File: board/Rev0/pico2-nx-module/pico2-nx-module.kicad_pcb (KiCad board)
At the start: 2 copper layers, 89 x 83 mm, 242 parts, among them IC1 LP5810ADSDR, J1 USB_C_Receptacle_USB2.0, J10 FTSH-105-01-L-DV-007-K, J11 Conn_02x06_Odd_Even, J12 Conn_02x03_Odd_Even, J13 Conn_02x03_Odd_Even, J14 Conn_02x03_Odd_Even, J15 Conn_02x03_Odd_Even, J16 Conn_02x06_Odd_Even, J17 Conn_02x06_Odd_Even, J18 100 mil, J2 SM03B-SRSS-TB, J3 SFV22R-2STE1HLF, J4 SFV22R-2STE1HLF, J5 Conn_02x06_Odd_Even, J6 Conn_02x06_Odd_Even, J7 SM04B-SRSS-TB, J8 Conn_02x06_Odd_Even, J9 SM04B-SRSS-TB, Q1 BSS84, SW1 CS1213AGF260, SW2 CS1213AGF260, U1 MIC2005A-2YM5-TR, U10 W25Q32JVSSIQ, U11 RP2350_80QFN, U14 74LV4066, U15 TXS0108EPW, U16 TXS0108EPW, U17 SN74CB3Q3257, U2 MIC2005A-2YM5-TR, U3 LIFCL-17-7MG121C, U4 W25Q128JVSSIQ, U5 APS6408L-OBM-BA, U8 TXS0108EPW, U9 APS6404L-3SQN-SN, Y1 SG-210STF 24.0000ML0, Y2 ABM8-272-T3

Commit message: layout update
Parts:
- removed C1, C2, C4, C5, C75, C82: 10u, Capacitor_SMD:C_0402_1005Metric
- removed C16, C17, C19, C49, C52, C59, C60, C63, C65, C66, C67, C69, C70, C71, C72, C73, C74, C77, C78, C79, C80, C85: 0.1u, Capacitor_SMD:C_0201_0603Metric
- removed C50, C53, C54, C57, C58, C61, C62, C64, C68: 4.7u, Capacitor_SMD:C_0402_1005Metric
- removed C55, C56: 15p, Capacitor_SMD:C_0201_0603Metric
- removed D1, D2, D6: 1N5819WS, Diode_SMD:D_SOD-323
- removed D10: PRTR5V0U2X, Package_TO_SOT_SMD:SOT-143
- removed D3, D5: LTST-C191KGKT, LED_SMD:LED_0603_1608Metric
- removed D4, D7: MHPA1010RGBDT, Piconx3_lib:LED_Cree-PLCC4_1x1mm_CW
- removed FB1: BLM15AG121SN1D, jrt:IND_BLM15_0402_MUR-M
- removed IC1: LP5810ADSDR, jrt:DSD0008B-MFG
- removed J1: USB_C_Receptacle_USB2.0, Connector_USB:USB_C_Receptacle_HRO_TYPE-C-31-M-12
- removed J10: FTSH-105-01-L-DV-007-K, Piconx3_lib:SAMTEC_FTSH-105-X-X-DV-007-P-X_cust
- removed J11, J16, J17, J5, J6, J8: Conn_02x06_Odd_Even, jrt:SAMTEC_HMTSW-106-XX-X-D-XXX
- removed J12, J13, J14, J15: Conn_02x03_Odd_Even, Connector_PinHeader_2.54mm:PinHeader_2x03_P2.54mm_Vertical
- removed J18: 100 mil, Connector_PinHeader_2.54mm:PinHeader_2x05_P2.54mm_Vertical
- removed J4: SFV22R-2STE1HLF, Piconx3_lib:AMPHENOL_SFV22R-2STE1HLF
- removed J7, J9: SM04B-SRSS-TB, Connector_JST:JST_SH_SM04B-SRSS-TB_1x04-1MP_P1.00mm_Horizontal
- removed JP1, JP2, JP3, JP6, JP7: SolderJumper_3_Bridged12, Jumper:SolderJumper-3_P1.3mm_Bridged12_RoundedPad1.0x1.5mm
- removed JP10, JP11, JP12, JP13, JP14, JP4, JP5, JP8, JP9: SolderJumper_2_Bridged, Jumper:SolderJumper-2_P1.3mm_Bridged_RoundedPad1.0x1.5mm
- removed JP15: SolderJumper_2_Open, Jumper:SolderJumper-2_P1.3mm_Open_RoundedPad1.0x1.5mm
- removed L1, L2: 1u, Piconx3_lib:DFE201610E
- removed L4: 3.3u, Piconx3_lib:INDC2016X100N
- removed PS1, PS2, PS3: AP61100QZ6-7, Piconx3_lib:SOT50P160X60-6N
- removed PTC1: MF-FSMF035X-2, Resistor_SMD:R_0603_1608Metric
- removed Q1: BSS84, Package_TO_SOT_SMD:SOT-23
- removed R1, R2, R28, R29, R30, R31, R32, R4, R40, R42, R50, R55, R60, R63, R70, R71: 10K, Resistor_SMD:R_0402_1005Metric
- removed R10, R13, R15, R16, R5, R59, R6, R7: 4.7K, Resistor_SMD:R_0402_1005Metric
- removed R11, R41, R49: 2.2K, Resistor_SMD:R_0402_1005Metric
- removed R14, R21, R23, R25, R52, R61, R64, R65, R66, R67, R75: 200K, Resistor_SMD:R_0402_1005Metric
- removed R17, R35: DNF, Resistor_SMD:R_0402_1005Metric
- removed R19, R20: 0, Resistor_SMD:R_0402_1005Metric
- removed R22: 100K, Resistor_SMD:R_0402_1005Metric
- removed R24: 44.2K, Resistor_SMD:R_0402_1005Metric
- removed R27, R44, R53, R54: 27, Resistor_SMD:R_0402_1005Metric
- removed R34, R45, R46, R47, R48, R56, R57, R58: 1K, Resistor_SMD:R_0402_1005Metric
- removed R36, R38: 56K, Resistor_SMD:R_0402_1005Metric
- removed R37, R39: 5.1K, Resistor_SMD:R_0402_1005Metric
- removed R43, R72, R76, R77, R79: 100, Resistor_SMD:R_0402_1005Metric
- removed R68, R69: 200, Resistor_SMD:R_0402_1005Metric
- removed SW1, SW2: CS1213AGF260, Piconx3_lib:CS1213AGF260
- removed TP1: 1V8, TestPoint:TestPoint_Pad_1.0x1.0mm
- removed TP2: 3V3, TestPoint:TestPoint_Pad_1.0x1.0mm
- removed TP5, TP6: TestPoint, TestPoint:TestPoint_Pad_1.0x1.0mm
- removed U1, U2: MIC2005A-2YM5-TR, jrt:SOT-23-5_M5_MCH
- removed U10: W25Q32JVSSIQ, jrt:SOIC-8_5P28X5P28_WIN
- removed U11: RP2350_80QFN, Piconx3_lib:QFN40P1000X1000X90-81N-D
- removed U14: 74LV4066, Package_SO:SO-14_3.9x8.65mm_P1.27mm
- removed U15, U16, U8: TXS0108EPW, Package_SO:TSSOP-20_4.4x6.5mm_P0.65mm
- removed U17: SN74CB3Q3257, jrt:SOP65P640X120-16N
- removed U9: APS6404L-3SQN-SN, Package_SO:SOIC-8_3.9x4.9mm_P1.27mm
- removed Y1: SG-210STF 24.0000ML0, Oscillator:Oscillator_SMD_SeikoEpson_SG210-4Pin_2.5x2.0mm
- removed Y2: ABM8-272-T3, Crystal:Crystal_SMD_3225-4Pin_3.2x2.5mm
- added FB9: BLM15AG121SN1D, pico:IND_BLM15_0402_MUR-M, B.Cu at (130.1, 96.1)
- added R78: 4.7K, Resistor_SMD:R_0402_1005Metric, B.Cu at (107.1, 100.3)
- added U13: APS6408L-OBM-BA, pico:BGA24_APS6408L-3OBM-BA_APY, F.Cu at (110.4, 101.5)
- C10, C12, C13, C14, C47, C7, C76, C8, C9: moved to B.Cu
- C11: value 0.1u -> 10u; footprint Capacitor_SMD:C_0201_0603Metric -> Capacitor_SMD:C_0402_1005Metric; moved to B.Cu
- C15, C83, C84: value 10u -> 0.1u; footprint Capacitor_SMD:C_0402_1005Metric -> Capacitor_SMD:C_0201_0603Metric; moved to B.Cu
- C18: value 10u -> 0.1u; footprint Capacitor_SMD:C_0402_1005Metric -> Capacitor_SMD:C_0201_0603Metric; moved to F.Cu
- C20, C32, C41, C42, C43, C48, C51: value 0.1u -> 10u; footprint Capacitor_SMD:C_0201_0603Metric -> Capacitor_SMD:C_0402_1005Metric
- C23, C35, C36: value 10u -> 0.1u; footprint Capacitor_SMD:C_0402_1005Metric -> Capacitor_SMD:C_0201_0603Metric
- C26: value 4.7u -> 10u
- C27: value 10u -> 2.2u
- C30, C38, R26, TP3: moved to F.Cu
- C31: value 0.1u -> 10u; footprint Capacitor_SMD:C_0201_0603Metric -> Capacitor_SMD:C_0402_1005Metric; moved to F.Cu
- C6: value 10u -> 33p; footprint Capacitor_SMD:C_0402_1005Metric -> Capacitor_SMD:C_0201_0603Metric
- C81: value 4.7u -> 0.1u; footprint Capacitor_SMD:C_0402_1005Metric -> Capacitor_SMD:C_0201_0603Metric; moved to B.Cu
- FB2, FB5: footprint jrt:IND_BLM15_0402_MUR-M -> pico:IND_BLM15_0402_MUR-M; moved to F.Cu
- FB3, FB4, FB6, FB7, FB8: footprint jrt:IND_BLM15_0402_MUR-M -> pico:IND_BLM15_0402_MUR-M
- J2: value SM03B-SRSS-TB -> DF40C-60DP-0.4V(51); footprint Connector_JST:JST_SH_SM03B-SRSS-TB_1x03-1MP_P1.00mm_Horizontal -> pico:DF40C60DP04V51; moved to B.Cu
- J3: value SFV22R-2STE1HLF -> DF40C-60DP-0.4V(51); footprint Piconx3_lib:AMPHENOL_SFV22R-2STE1HLF -> pico:DF40C60DP04V51; moved to B.Cu
- L3: footprint Piconx3_lib:DFE201610E -> pico:DFE201610E
- R12, R3: value 10K -> 27
- R18: value 0 -> 200K; moved to F.Cu
- R33: value 27 -> 4.7K
- R51: value 5.1K -> 4.7K; moved to B.Cu
- R62: value 10K -> 4.7K; moved to B.Cu
- R8: value 4.7K -> DNF
- U3: footprint jrt:BGA121N50P11X11_600X600X100 -> pico:BGA121N50P11X11_600X600X100
- U4: value W25Q128JVSSIQ -> W25Q128JVPIQ; footprint jrt:SOIC-8_5P28X5P28_WIN -> Package_SON:WSON-8-1EP_6x5mm_P1.27mm_EP3.4x4.3mm
- U5: value APS6408L-OBM-BA -> AP61102QZ6-7; footprint jrt:BGA24_APS6408L-3OBM-BA_APY -> Package_TO_SOT_SMD:SOT-563
- moved R8 85.9 mm to (133.4, 90.9), turned to -90 degrees
- moved C11 72.4 mm to (124.8, 98.4), turned to -90 degrees
- moved R3 67.6 mm to (108.5, 94.2), turned to 90 degrees
- moved C12 65.7 mm to (119.3, 94.2), turned to 180 degrees
- moved C14 65.1 mm to (118.8, 97.2), turned to 180 degrees
- moved C13 64.2 mm to (118.1, 94.2), turned to 180 degrees
- moved C47 62.2 mm to (123.0, 94.7), turned to -90 degrees
- moved C7 61.9 mm to (123.8, 98.4), turned to -90 degrees
- moved FB2 60.1 mm to (130.1, 96.1)
- moved R12 59.6 mm to (113.6, 89.2), turned to 90 degrees
- moved C15 57.9 mm to (122.1, 96.4), turned to 90 degrees
- moved C38 56.8 mm to (118.5, 90.2), turned to -90 degrees
- moved C39 55.5 mm to (132.9, 92.7), turned to 0 degrees
- moved R51 55.3 mm to (110.2, 93.8), turned to 0 degrees
- moved C10 55.1 mm to (118.6, 98.1), turned to 180 degrees
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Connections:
- C10 pad 1: P1V8D_FPGA -> PVIO3_FPGA
- C11 pad 1: P3V3D_FPGA -> PVIO5_FPGA
- C13 pad 1: P1V8D_FPGA -> PVIO1_FPGA
- C14 pad 1: P1V8D_FPGA -> PVIO3_FPGA
- C15 pad 1: P1V8D_FPGA -> PVIO5_FPGA
- C18 pad 1: P1V8D_FPGA -> P3V3D_FPGA
- C23 pad 1: P1VD_FPGA -> P1V8D_FPGA
- C24 pad 1: Net-(U3F-VCCPLLDPHY0) -> P1VD_FPGA
- C25 pad 1: Net-(U3F-VCCDPHY0) -> Net-(U3F-VCCPLLDPHY0)
- C26 pad 1: Net-(U3G-VCCPLLDPHY1) -> Net-(U3F-VCCDPHY0)
- C27 pad 1: Net-(U3G-VCCDPHY1) -> Net-(U3G-VCCPLLDPHY1)
- C28 pad 1: P1VD_FPGA -> Net-(U3G-VCCDPHY1)
- C29 pad 1: GND -> P1V8D_FPGA
- C29 pad 2: Net-(U3F-VCCADPHY0) -> GND
- C3 pad 1: P5VD -> P5VD_AON
- C30 pad 2: Net-(U3G-VCCADPHY1) -> Net-(U3F-VCCADPHY0)
- C31 pad 1: Net-(U3F-VCCPLLDPHY0) -> GND
- C31 pad 2: GND -> Net-(U3G-VCCADPHY1)
- C32 pad 1: Net-(U3F-VCCDPHY0) -> P1VD_FPGA
- C33 pad 1: Net-(U3G-VCCPLLDPHY1) -> Net-(U3F-VCCPLLDPHY0)
- C34 pad 1: Net-(U3G-VCCDPHY1) -> Net-(U3F-VCCDPHY0)
- C35 pad 1: P1VD_FPGA -> Net-(U3G-VCCPLLDPHY1)
- C36 pad 1: /FPGA/PVCCAUX -> Net-(U3G-VCCDPHY1)
- C39 pad 1: Net-(U3H-VCCAUXH5) -> P1VD_FPGA
- C41 pad 1: P1VD_FPGA -> P1V8D_FPGA
- C43 pad 1: P1VD_FPGA -> /FPGA/PVCCAUX
- C44 pad 1: /FPGA/PVCCAUX -> P1VD_FPGA
- C45 pad 1: P1VD_FPGA -> P1V8D_FPGA
- C46 pad 1: /FPGA/PVCCAUX -> Net-(U3H-VCCAUXH5)
- C47 pad 1: /FPGA/PVCCAUX -> P1VD_FPGA
- C48 pad 1: P1V8D -> P1VD_FPGA
- C51 pad 1: P3V3D -> P1VD_FPGA
- C6 pad 1: P3V3D -> P1VD_FPGA
- C6 pad 2: GND -> Net-(U5-FB)
- C7 pad 1: P3V3D_FPGA -> PVIO5_FPGA
- C76 pad 1: P3V3D -> /FPGA/PVCCAUX
- C81 pad 1: GND -> P1VD_FPGA
- C81 pad 2: P1V8D_FPGA -> GND
- C83 pad 1: P1V8D_FPGA -> /FPGA/PVCCAUX
- C84 pad 1: P1V8D_FPGA -> /FPGA/PVCCAUX
- C9 pad 1: P1V8D_FPGA -> PVIO1_FPGA
- FB2 pad 2: Net-(U3G-VCCADPHY1) -> Net-(U3F-VCCADPHY0)
- FB5 pad 1: P1VD_FPGA -> P1V8D_FPGA
- FB5 pad 2: Net-(U3G-VCCPLLDPHY1) -> Net-(U3G-VCCADPHY1)
- FB6 pad 2: Net-(U3G-VCCDPHY1) -> Net-(U3G-VCCPLLDPHY1)
- FB7 pad 1: P1V8D_FPGA -> P1VD_FPGA
- FB7 pad 2: /FPGA/PVCCAUX -> Net-(U3G-VCCDPHY1)
- FB8 pad 2: Net-(U3H-VCCAUXH5) -> /FPGA/PVCCAUX
- J2 pad 1: Net-(J2-Pin_1) -> /FPGA/HSTX7
- J2 pad 2: GND -> /FPGA/SHARED_PMOD_B5
- J2 pad 3: Net-(J2-Pin_3) -> /FPGA/HSTX6
- J3 pad 1: P3V3D_FPGA -> /FPGA/SHUTDOWNn
- J3 pad 10: GND -> /FPGA/RGB_MIPI.D1-
- J3 pad 11: /Connectors/EXT_MIPI.D2+ -> PVIO1_FPGA
- J3 pad 12: /Connectors/EXT_MIPI.D2- -> /FPGA/RGB_MIPI.D1+
- J3 pad 13: GND -> P3V3D_FPGA
- J3 pad 14: /Connectors/EXT_MIPI.CLK+ -> GND
- J3 pad 15: /Connectors/EXT_MIPI.CLK- -> /FPGA/FPGA_EN
- J3 pad 16: GND -> /FPGA/RGB_MIPI.CLK-
- J3 pad 17: /Connectors/EXT_MIPI.D1+ -> /FPGA/DONE
- J3 pad 18: /Connectors/EXT_MIPI.D1- -> /FPGA/RGB_MIPI.CLK+
- J3 pad 19: GND -> /FPGA/EXT_QSPI.SCK
- J3 pad 2: /Connectors/SDA0 -> GND
- J3 pad 20: /Connectors/EXT_MIPI.D0+ -> GND
- J3 pad 21: /Connectors/EXT_MIPI.D0- -> /FPGA/FLASH_CSn
- J3 pad 22: GND -> /FPGA/RGB_MIPI.D2-
- J3 pad 3: /Connectors/SCL0 -> P5VD_AON
- J3 pad 4: GND -> /FPGA/RGB_MIPI.D0-
- J3 pad 5: /Connectors/FPC_IO.LED_EN -> PVIO5_FPGA
- J3 pad 6: /Connectors/FPC_IO.PWR_EN -> /FPGA/RGB_MIPI.D0+
- J3 pad 7: GND -> P1V8D_FPGA
- J3 pad 8: /Connectors/EXT_MIPI.D3+ -> GND
- J3 pad 9: /Connectors/EXT_MIPI.D3- -> PVIO3_FPGA
- L3 pad 1: Net-(PS3-SW) -> Net-(U5-SW)
- L3 pad 2: P3V3D -> P1VD_FPGA
- R12 pad 1: /FPGA/QSPI.CSn -> Net-(U3B-PR9B)
- R12 pad 2: P1V8D_FPGA -> /FPGA/MIPI_IO.LED_EN
- R18 pad 1: Net-(PS2-OUT) -> Net-(U5-FB)
- R18 pad 2: Net-(JP13-B) -> P1VD_FPGA
- R26 pad 2: Net-(PS2-FB) -> Net-(U5-FB)
- R3 pad 1: /Connectors/EXT_SPI.CSn -> Net-(U3A-PT59A/MCLK/PCLKT0_0)
- R3 pad 2: P3V3D_FPGA -> /FPGA/EXT_QSPI.SCK
- R33 pad 1: Net-(Y1-OUT) -> /FPGA/EXT_QSPI.SD2
- R33 pad 2: /FPGA/FPGA_CLK -> P3V3D_FPGA
- R51 pad 1: /Connectors/USB_BOOTn -> /FPGA/EXT_QSPI.SD3
- R51 pad 2: /RP2350/RP_BUTTONn -> P3V3D_FPGA
- R62 pad 1: P3V3D_FPGA -> /FPGA/SRAM_CEN
- R62 pad 2: /Connectors/DONE -> P1V8D_FPGA
- R8 pad 1: /Connectors/I2C0.SCL -> Net-(U5-PG)
- R8 pad 2: P3V3D -> P1VD_FPGA
- R9 pad 1: /FPGA/JTAG_EN -> /FPGA/FLASH_CSn
- R9 pad 2: GND -> P3V3D_FPGA
- TP3 pad 1: Net-(JP13-B) -> P1VD_FPGA
- U3 pad A10: /Connectors/RGB_MIPI.D3- -> /FPGA/RGB_MIPI.D3-
- U3 pad A11: /Connectors/RGB_MIPI.D3+ -> /FPGA/RGB_MIPI.D3+
- U3 pad A5: /Connectors/EXT_MIPI.D3+ -> /FPGA/EXT_MIPI.D3+
- U3 pad A6: /Connectors/EXT_MIPI.D1+ -> /FPGA/EXT_MIPI.D1+
- U3 pad A7: /Connectors/EXT_MIPI.CLK+ -> /FPGA/EXT_MIPI.CLK+
- U3 pad A8: /Connectors/EXT_MIPI.D0+ -> /FPGA/EXT_MIPI.D0+
- U3 pad A9: /Connectors/EXT_MIPI.D2+ -> /FPGA/EXT_MIPI.D2+
- U3 pad B10: /Connectors/RGB_MIPI.D1- -> /FPGA/RGB_MIPI.D1-
- U3 pad B11: /Connectors/RGB_MIPI.D1+ -> /FPGA/RGB_MIPI.D1+
- U3 pad B2: /Connectors/FPGA_PMOD2 -> /FPGA/FPGA_PMOD0
- U3 pad B3: /Connectors/FPGA_PMOD1 -> /FPGA/FPGA_PMOD3
- U3 pad B5: /Connectors/EXT_MIPI.D3- -> /FPGA/EXT_MIPI.D3-
- U3 pad B6: /Connectors/EXT_MIPI.D1- -> /FPGA/EXT_MIPI.D1-
- U3 pad B7: /Connectors/EXT_MIPI.CLK- -> /FPGA/EXT_MIPI.CLK-
- U3 pad B8: /Connectors/EXT_MIPI.D0- -> /FPGA/EXT_MIPI.D0-
- U3 pad B9: /Connectors/EXT_MIPI.D2- -> /FPGA/EXT_MIPI.D2-
- U3 pad C10: /Connectors/RGB_MIPI.CLK- -> /FPGA/RGB_MIPI.CLK-
- U3 pad C11: /Connectors/RGB_MIPI.CLK+ -> /FPGA/RGB_MIPI.CLK+
- U3 pad C2: /Connectors/FPGA_PMOD6 -> /FPGA/FPGA_PMOD4
- U3 pad C3: /Connectors/FPGA_PMOD5 -> /FPGA/FPGA_PMOD7
- U3 pad D1: /Connectors/I2C1.SDA -> Net-(U3B-PR9B)
- U3 pad D10: /Connectors/RGB_MIPI.D0- -> /FPGA/RGB_MIPI.D0-
- U3 pad D11: /Connectors/RGB_MIPI.D0+ -> /FPGA/RGB_MIPI.D0+
- U3 pad D2: P3V3D_FPGA -> PVIO1_FPGA
- U3 pad D5: /Connectors/I2C_IRQn -> /FPGA/EXT_QSPI.SD2
- U3 pad D6: /Connectors/EXT_SPI.MOSI -> /FPGA/EXT_QSPI.MOSI
- U3 pad D7: /Connectors/DONE -> /FPGA/DONE
- U3 pad D8: /Connectors/MULTI_FN -> /FPGA/FPGA_PMOD6
- U3 pad E10: /Connectors/RGB_MIPI.D2- -> /FPGA/RGB_MIPI.D2-
- U3 pad E11: /Connectors/RGB_MIPI.D2+ -> /FPGA/RGB_MIPI.D2+
- U3 pad E2: /Connectors/I2C1.SCL -> /FPGA/MULTI_FN
- U3 pad E3: /Connectors/FPGA_PMOD4 -> /FPGA/EXT_QSPI.CSn
- U3 pad E4: /Connectors/FPGA_PMOD0 -> /FPGA/EXT_QSPI.SD3
- U3 pad E5: /Connectors/EXT_SPI.MISO -> /FPGA/EXT_QSPI.MISO
- U3 pad E8: /Connectors/EXT_SPI.CSn -> /FPGA/FPGA_PMOD2
- U3 pad F1: /Connectors/FPGA_PMOD7 -> /FPGA/FPGA_PMOD5
- U3 pad F2: /Connectors/FPGA_PMOD3 -> /FPGA/FPGA_PMOD1
- U3 pad G1: /FPGA/HSTX7 -> /FPGA/SHARED_PMOD_B5
- U3 pad G10: /Connectors/SHARED_PMOD_A0 -> /FPGA/SCL1
- U3 pad G11: /Connectors/SHARED_PMOD_A2 -> /FPGA/SDA1
- U3 pad G2: /FPGA/HSTX6 -> /FPGA/SHARED_PMOD_B7
- U3 pad G4: /FPGA/FPGA_CLK -> /FPGA/SHARED_PMOD_A4
- U3 pad H1: /FPGA/HSTX4 -> /FPGA/SHARED_PMOD_B4
- U3 pad H10: /Connectors/SHARED_PMOD_A1 -> /FPGA/SCL0
- U3 pad H11: /Connectors/SHARED_PMOD_A3 -> /FPGA/SDA0
- U3 pad H2: /FPGA/HSTX5 -> /FPGA/SHARED_PMOD_B6
- U3 pad H4: unconnected-(U3C-PB60B/PCLKC3_1/ADC_CN6-PadH4) -> /FPGA/SHARED_PMOD_A6
- U3 pad J1: /FPGA/HSTX2 -> /FPGA/SHARED_PMOD_B3
- U3 pad J10: /Connectors/SHARED_PMOD_A6 -> /FPGA/IRQn
- U3 pad J11: /Connectors/SHARED_PMOD_A4 -> /FPGA/FPGA_CLK
- U3 pad J2: /FPGA/HSTX3 -> /FPGA/SHARED_PMOD_B1
- U3 pad J4: /FPGA/FPC_IO_1V8.LED_EN -> /FPGA/SHARED_PMOD_A3
- U3 pad J7: /Connectors/SHARED_PMOD_B6 -> /FPGA/HSTX5
- U3 pad J8: unconnected-(U3D-PB42A/PCLKT4_3-PadJ8) -> /FPGA/PB42A
- U3 pad J9: P1V8D_FPGA -> PVIO5_FPGA
- U3 pad K1: /FPGA/HSTX0 -> /FPGA/SHARED_PMOD_B2
- U3 pad K10: /Connectors/SHARED_PMOD_B5 -> /FPGA/HSTX7
- U3 pad K11: /Connectors/SHARED_PMOD_B3 -> /FPGA/HSTX2
- U3 pad K2: /FPGA/HSTX1 -> /FPGA/SHARED_PMOD_B0
- U3 pad K3: P1V8D_FPGA -> PVIO3_FPGA
- U3 pad K4: unconnected-(U3C-PB58B/ADC_CN7-PadK4) -> /FPGA/SHARED_PMOD_A1
- U3 pad K6: /Connectors/SHARED_PMOD_B0 -> /FPGA/HSTX1
- U3 pad K7: /Connectors/SHARED_PMOD_B4 -> /FPGA/HSTX4
- U3 pad K8: unconnected-(U3D-PB42B/PCLKC4_3-PadK8) -> /FPGA/PB42B
- U3 pad K9: unconnected-(U3D-PB40B-PadK9) -> /FPGA/PB40B
- U3 pad L1: unconnected-(U3C-PB62B/ADC_CN9-PadL1) -> /FPGA/SHARED_PMOD_A5
- U3 pad L10: /Connectors/SHARED_PMOD_B7 -> /FPGA/HSTX6
- U3 pad L11: /Connectors/SHARED_PMOD_B1 -> /FPGA/HSTX3
- U3 pad L2: unconnected-(U3C-PB62A/ADC_CP9-PadL2) -> /FPGA/SHARED_PMOD_A7
- U3 pad L3: /FPGA/FPC_IO_1V8.PWR_EN -> /FPGA/SHARED_PMOD_A0
- U3 pad L4: /FPGA/QSPI.CSn -> /FPGA/SHARED_PMOD_A2
- U3 pad L6: /Connectors/SHARED_PMOD_B2 -> /FPGA/HSTX0
- U3 pad L7: /Connectors/SHARED_PMOD_A7 -> /FPGA/QSPI.CSn
- U3 pad L8: /Connectors/SHARED_PMOD_A5 -> /FPGA/MIPI_IO.PWR_EN
- U3 pad L9: unconnected-(U3D-PB40A/VREF4_1-PadL9) -> /FPGA/PB40A
- U4 pad 2: /Connectors/EXT_SPI.MISO -> /FPGA/EXT_QSPI.MISO
- U4 pad 3: Net-(U4-IO2) -> /FPGA/EXT_QSPI.SD2
- U4 pad 5: /Connectors/EXT_SPI.MOSI -> /FPGA/EXT_QSPI.MOSI
- U4 pad 6: /Connectors/EXT_SPI.SCK -> /FPGA/EXT_QSPI.SCK
- U4 pad 7: Net-(U4-IO3) -> /FPGA/EXT_QSPI.SD3
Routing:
- net GND: track 0.00 -> 55.9 mm, vias 10 -> 94
- net /FPGA/EXT_QSPI.MOSI: track 0.00 -> 43.9 mm, vias 0 -> 2
- net PVIO3_FPGA: track 0.00 -> 40.1 mm, vias 0 -> 3
- net /FPGA/EXT_QSPI.MISO: track 0.00 -> 38.6 mm, vias 0 -> 2
- net /FPGA/EXT_QSPI.SD2: track 0.00 -> 37.5 mm, vias 0 -> 3
- net /FPGA/EXT_QSPI.SD3: track 0.00 -> 37.5 mm, vias 0 -> 2
- net /FPGA/FPGA_PMOD7: track 0.00 -> 37.3 mm, vias 0 -> 4
- net P3V3D_FPGA: track 0.00 -> 37.1 mm, vias 2 -> 4
- net /FPGA/FPGA_PMOD3: track 0.00 -> 34.0 mm, vias 0 -> 4
- net /FPGA/FLASH_CSn: track 0.00 -> 34.0 mm, vias 1 -> 3
- net /FPGA/EXT_QSPI.SCK: track 0.00 -> 28.4 mm, vias 0 -> 1
- net /FPGA/RGB_MIPI.D2+: track 0.00 -> 25.4 mm, vias 0 -> 1
- net /FPGA/EXT_MIPI.D3+: track 0.00 -> 25.3 mm, vias 0 -> 1
- net /FPGA/RGB_MIPI.D2-: track 0.00 -> 25.1 mm, vias 0 -> 1
- net /FPGA/EXT_MIPI.D3-: track 0.00 -> 25.0 mm, vias 0 -> 1
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- added copper zone on In3.Cu, net /FPGA/PVCCAUX
- added copper zone on F.Cu, net GND
- added copper zone on In1.Cu, net GND
- added copper zone on F.Cu, net Net-(U5-SW)
- added copper zone on B.Cu, net P1V8D_FPGA
- added copper zone on In3.Cu, net P1V8D_FPGA
- added copper zone on B.Cu, net P1VD_FPGA
- added copper zone on F.Cu, net P1VD_FPGA
- added copper zone on In3.Cu, net P3V3D_FPGA
- added copper zone on F.Cu, net P5VD_AON
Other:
- board size 89 x 83 mm -> 30 x 30 mm
- copper layers 2 -> 6

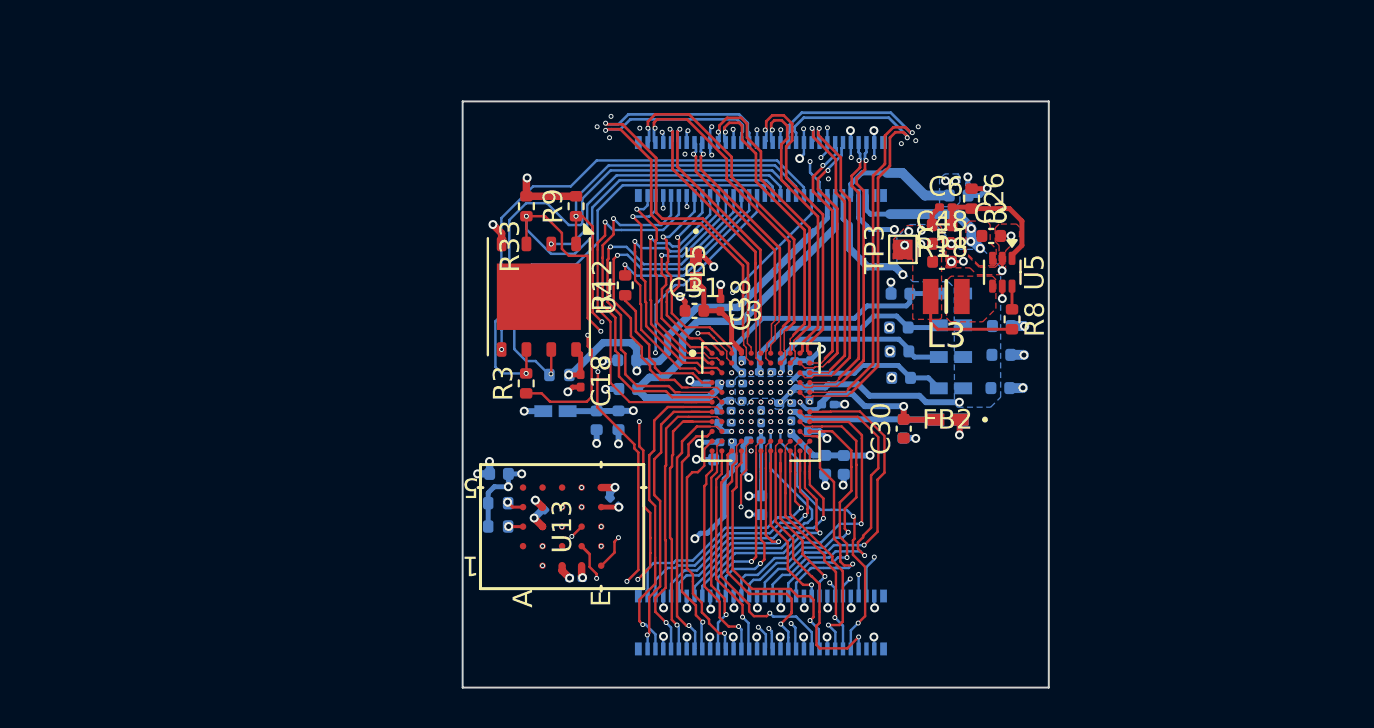
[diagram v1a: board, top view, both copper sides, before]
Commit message: Added a few more ground vias
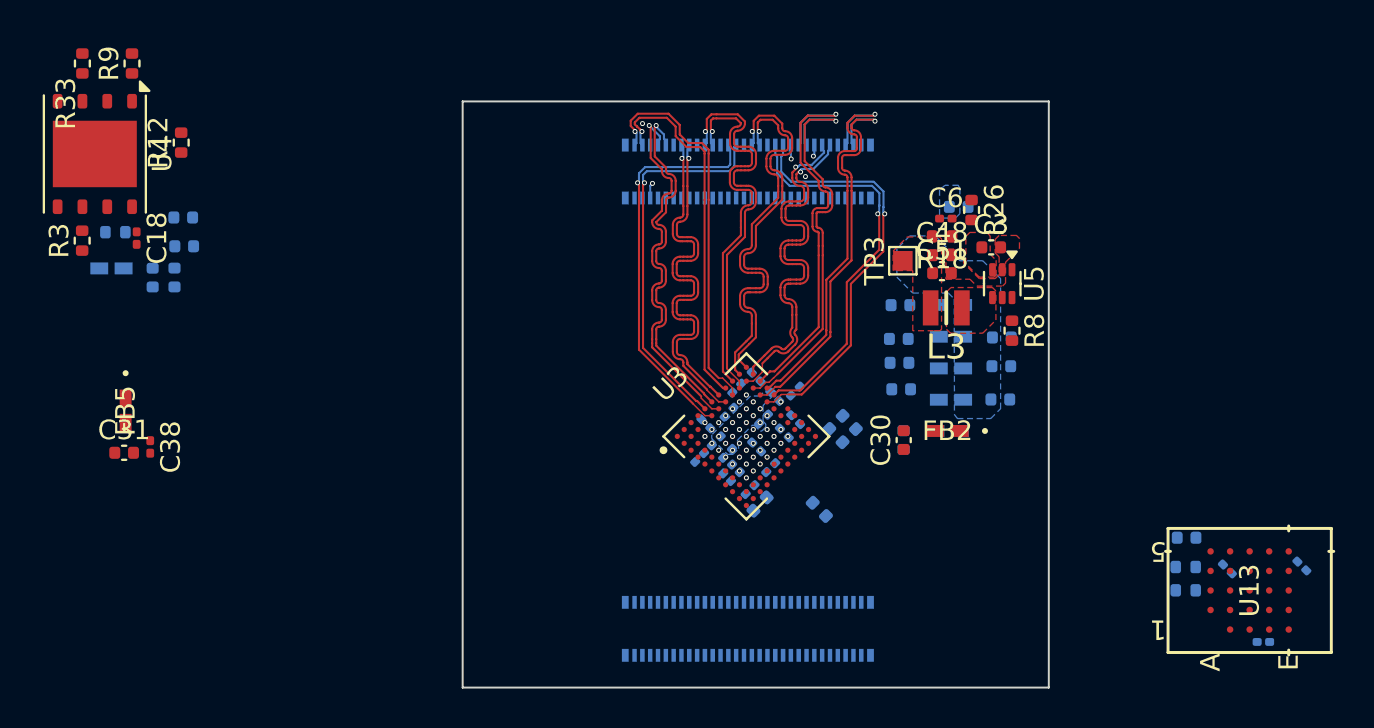
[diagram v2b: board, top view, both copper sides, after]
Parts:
- moved C21 35.3 mm to (146.3, 107.4)
- moved C20 35.3 mm to (142.3, 102.1)
- moved C22 35.3 mm to (144.4, 103.7)
- moved C23 35.3 mm to (148.2, 103.5)
- moved R62 35.3 mm to (142.3, 104.8)
- moved R78 35.3 mm to (142.3, 103.6)
- moved U13 35.3 mm to (145.6, 104.8)
- moved C31 30.1 mm to (88.0, 97.8)
- moved C38 30.1 mm to (89.3, 97.5)
- moved FB5 30.1 mm to (88.0, 95.6)
- moved C18 23.9 mm to (88.6, 86.8)
- moved C40 23.9 mm to (90.5, 88.8)
- moved C43 23.9 mm to (89.4, 88.8)
- moved C9 23.9 mm to (91.0, 87.2)
- moved FB8 23.9 mm to (87.3, 88.3)
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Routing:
- net GND: track 55.9 -> 2.10 mm, vias 94 -> 14
- net /FPGA/EXT_QSPI.MOSI: track 43.9 -> 0.00 mm, vias 2 -> 1
- net PVIO3_FPGA: track 40.1 -> 0.00 mm, vias 3 -> 0
- net /FPGA/EXT_QSPI.MISO: track 38.6 -> 0.00 mm, vias 2 -> 1
- net /FPGA/EXT_QSPI.SD2: track 37.5 -> 0.00 mm, vias 3 -> 1
- net /FPGA/EXT_QSPI.SD3: track 37.5 -> 0.00 mm, vias 2 -> 1
- net /FPGA/FPGA_PMOD7: track 37.3 -> 0.00 mm, vias 4 -> 1
- net /FPGA/FPGA_PMOD3: track 34.0 -> 0.00 mm, vias 4 -> 0
- net /FPGA/FLASH_CSn: track 34.0 -> 0.00 mm, vias 3 -> 1
- net /FPGA/EXT_QSPI.SCK: track 28.4 -> 0.00 mm, vias 1 -> 0
- net P3V3D_FPGA: track 37.1 -> 11.8 mm, vias 4 -> 1
- net Net-(U3A-PT59A/MCLK/PCLKT0_0): track 23.6 -> 0.00 mm, vias 2 -> 1
- net /FPGA/SRAM_DQ1: track 21.0 -> 0.00 mm, vias 2 -> 1
- net /FPGA/SRAM_CLK_P: track 20.9 -> 0.00 mm, vias 2 -> 1
- net PVIO1_FPGA: track 20.9 -> 0.00 mm, vias 1 -> 0
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
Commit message: Revert "Added a few more ground vias"
This reverts commit a71356e1e697da9fbd59bbea77a805aa35024750.
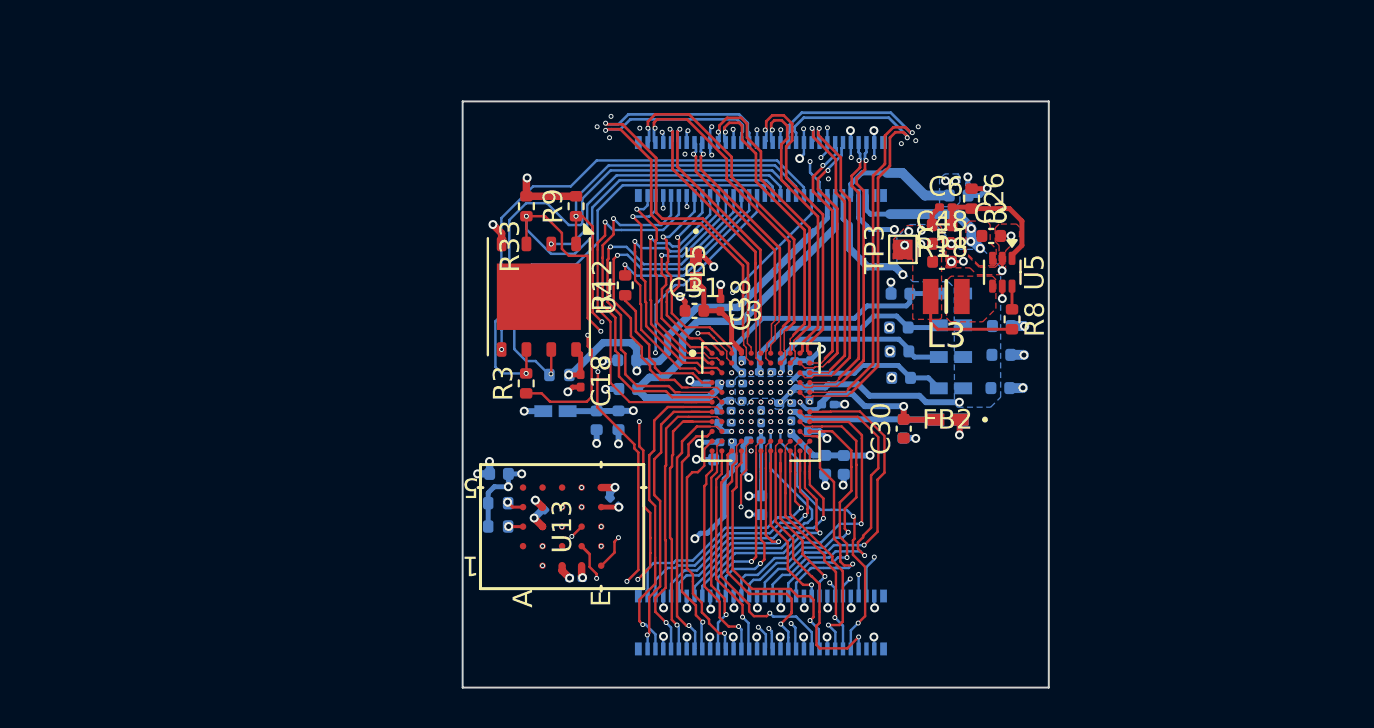
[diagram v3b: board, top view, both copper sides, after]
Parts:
- moved C21 35.3 mm to (111.1, 104.2)
- moved C20 35.3 mm to (107.2, 98.8)
- moved C22 35.3 mm to (109.2, 100.4)
- moved C23 35.3 mm to (113.1, 100.3)
- moved R62 35.3 mm to (107.1, 101.5)
- moved R78 35.3 mm to (107.1, 100.3)
- moved U13 35.3 mm to (110.4, 101.5)
- moved C31 30.1 mm to (117.2, 90.5)
- moved C38 30.1 mm to (118.5, 90.2)
- moved FB5 30.1 mm to (117.2, 88.3)
- moved C18 23.9 mm to (111.3, 94.1)
- moved C40 23.9 mm to (113.3, 96.1)
- moved C43 23.9 mm to (112.2, 96.1)
- moved C9 23.9 mm to (113.8, 94.5)
- moved FB8 23.9 mm to (110.0, 95.6)
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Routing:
- net GND: track 2.10 -> 55.9 mm, vias 14 -> 94
- net /FPGA/EXT_QSPI.MOSI: track 0.00 -> 43.9 mm, vias 1 -> 2
- net PVIO3_FPGA: track 0.00 -> 40.1 mm, vias 0 -> 3
- net /FPGA/EXT_QSPI.MISO: track 0.00 -> 38.6 mm, vias 1 -> 2
- net /FPGA/EXT_QSPI.SD2: track 0.00 -> 37.5 mm, vias 1 -> 3
- net /FPGA/EXT_QSPI.SD3: track 0.00 -> 37.5 mm, vias 1 -> 2
- net /FPGA/FPGA_PMOD7: track 0.00 -> 37.3 mm, vias 1 -> 4
- net /FPGA/FPGA_PMOD3: track 0.00 -> 34.0 mm, vias 0 -> 4
- net /FPGA/FLASH_CSn: track 0.00 -> 34.0 mm, vias 1 -> 3
- net /FPGA/EXT_QSPI.SCK: track 0.00 -> 28.4 mm, vias 0 -> 1
- net P3V3D_FPGA: track 11.8 -> 37.1 mm, vias 1 -> 4
- net Net-(U3A-PT59A/MCLK/PCLKT0_0): track 0.00 -> 23.6 mm, vias 1 -> 2
- net /FPGA/SRAM_DQ1: track 0.00 -> 21.0 mm, vias 1 -> 2
- net /FPGA/SRAM_CLK_P: track 0.00 -> 20.9 mm, vias 1 -> 2
- net PVIO1_FPGA: track 0.00 -> 20.9 mm, vias 0 -> 1
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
